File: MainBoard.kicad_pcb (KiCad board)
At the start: 4 copper layers, 110 x 100 mm, 99 parts, among them J1 USB B Mini, J5 Audio Out Port, P1 CARTRIDGE_SLOT, P2 FRONT_PANEL_CONNECTOR, P4 Multi AV Out, Q1 2SC4699, SW1 RESET, U1 S-CPU, U11 PST529D, U13 S-SMP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

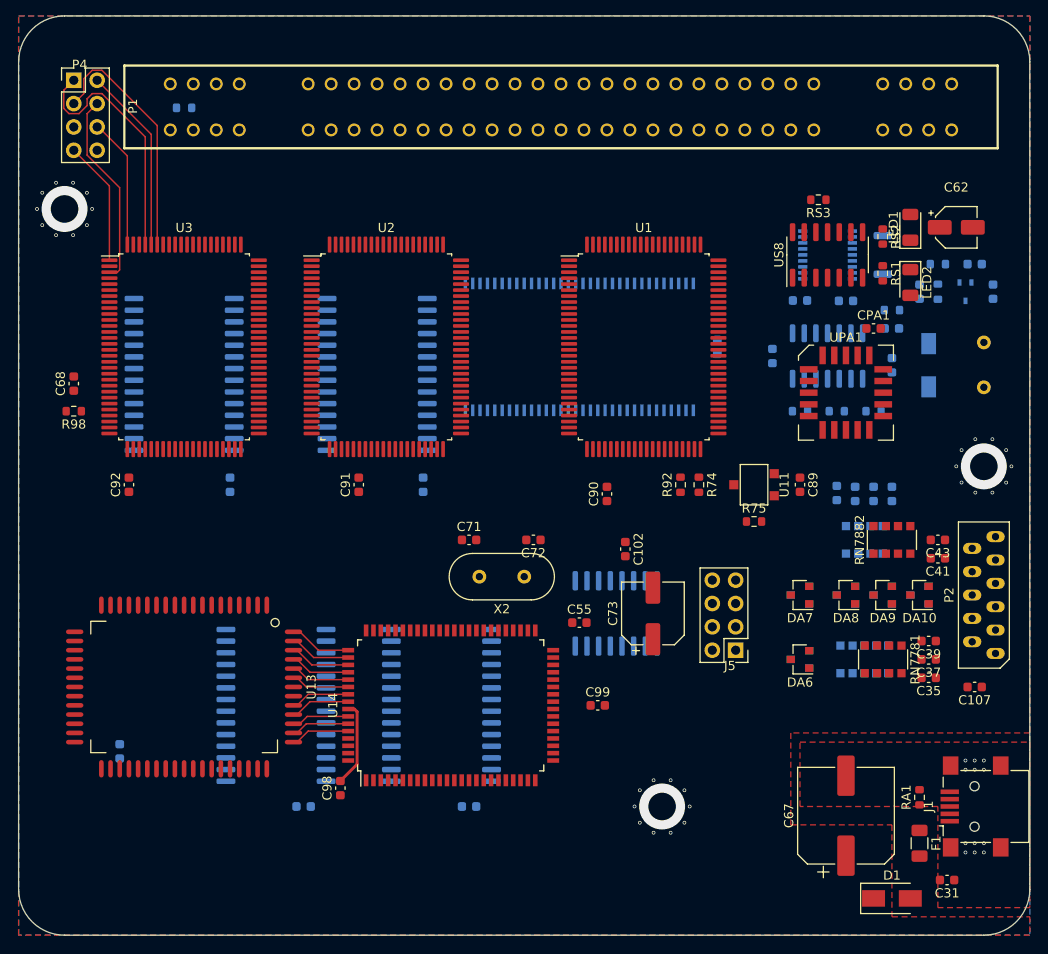
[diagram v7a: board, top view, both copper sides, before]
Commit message: Front/Back Silk Screen laid out
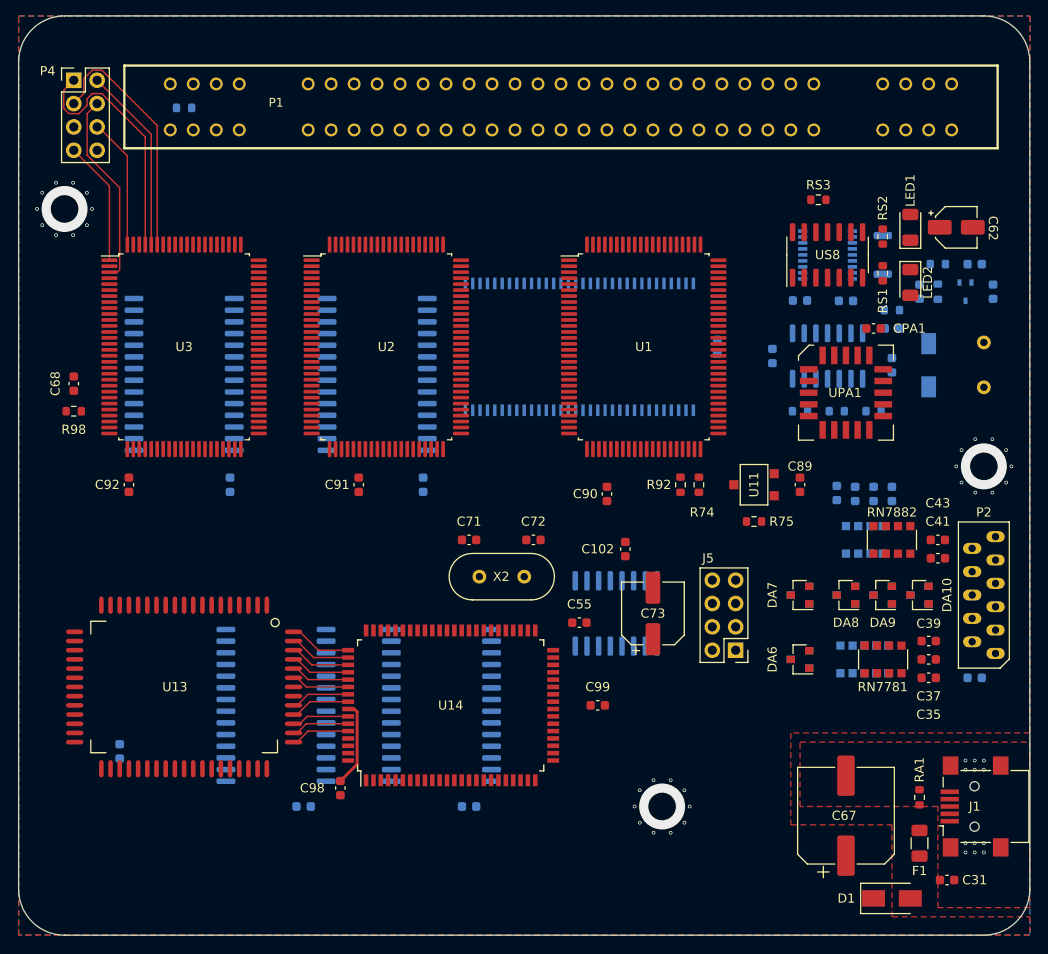
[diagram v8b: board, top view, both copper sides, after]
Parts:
- C107: moved to B.Cu
- moved C107 1.00 mm to (124.0, 122.0)
